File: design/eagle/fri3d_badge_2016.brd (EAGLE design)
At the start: 76.6 x 67.3 mm, 43 parts, among them Q1 MOSFET-NCHANNEL2N7002PW, U1 MCP73831

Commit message: added Fri3d Camp 2016 logo + silkscreen clean up
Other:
- board size 76.6 x 67.3 mm -> 76.5 x 67.4 mm
- board text removed: "Fri3d Camp 2016"

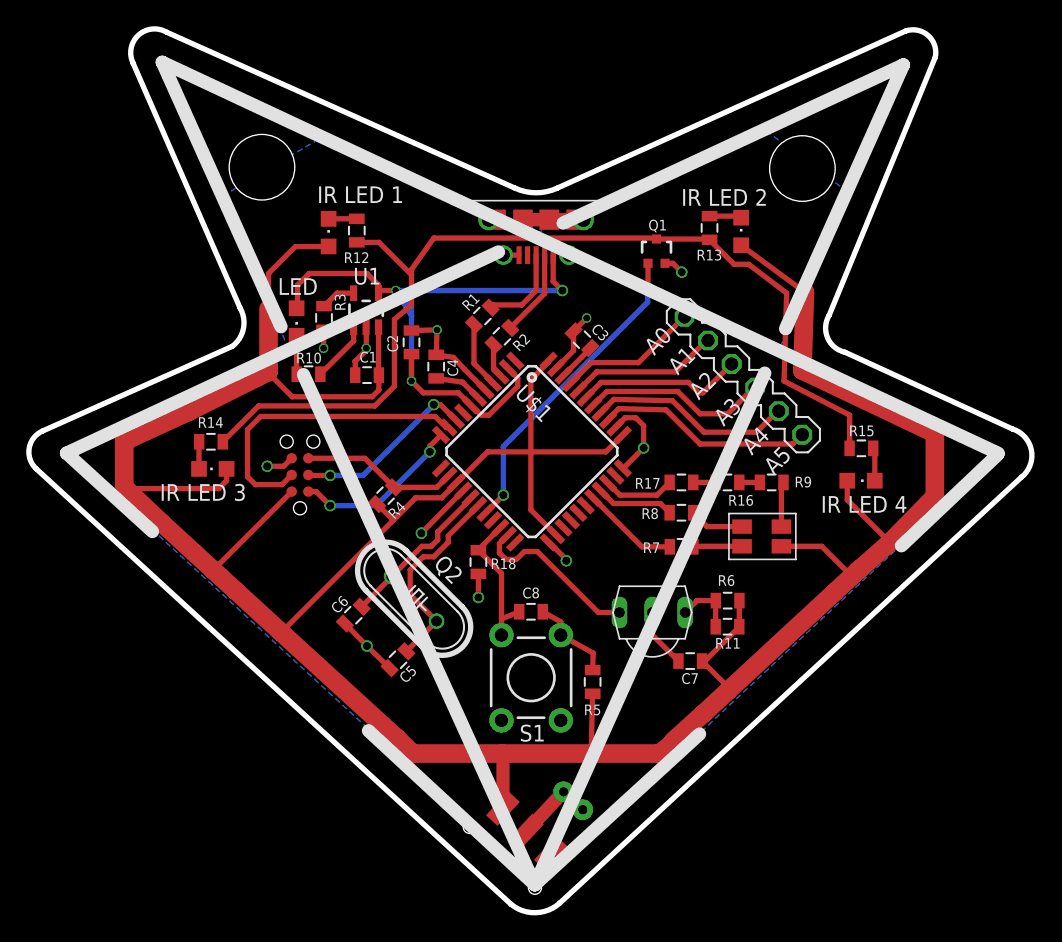
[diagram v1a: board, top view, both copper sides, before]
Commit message: IR powered by pin, added headers, cleaned up silk
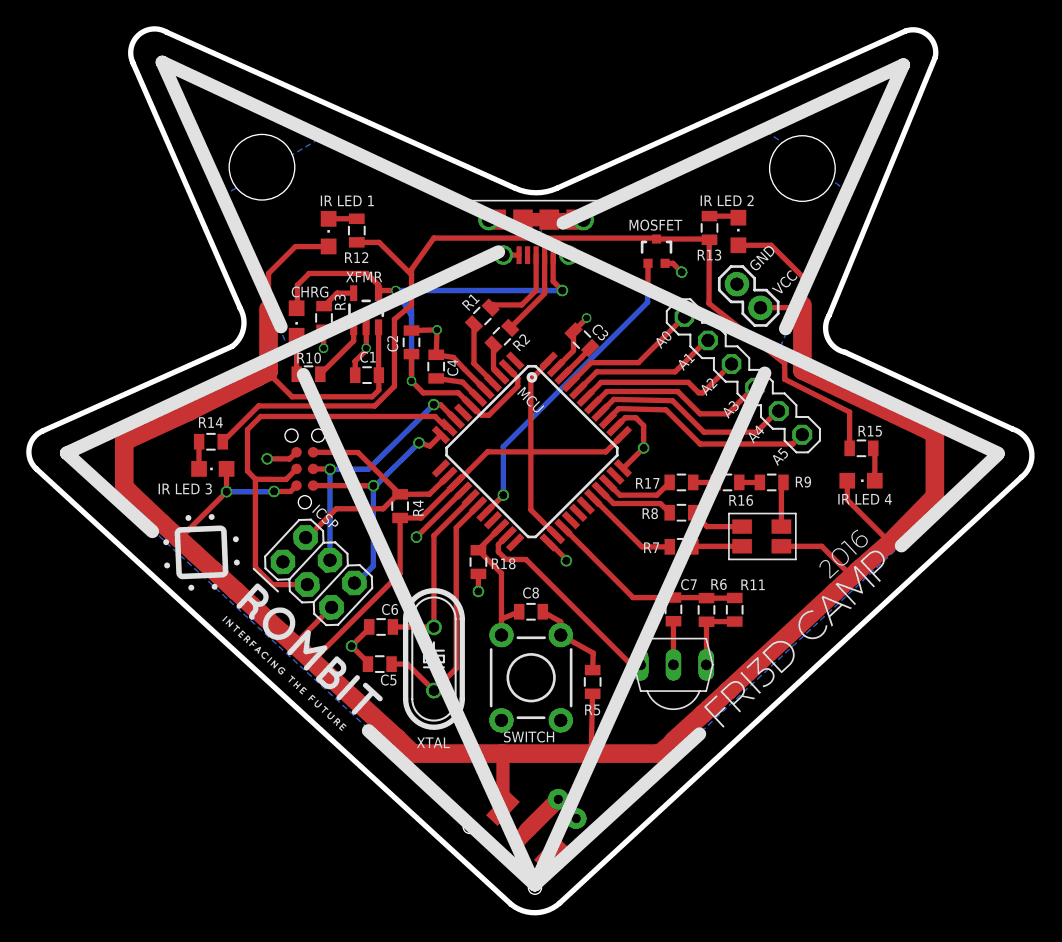
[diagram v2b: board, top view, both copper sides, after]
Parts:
- removed Q2: (no value), crystal:HC49/S
- added ICSP: (no value), SparkFun-Connectors:2X03
- added J2: (no value), SparkFun-Connectors:1X02
- added XTAL: (no value), crystal:HC49/S
- CHRGLED: value LED -> CHRG
- J3: device SparkFun-Connectors:JST-2-PTH-VERT -> SparkFun-Connectors:JST-2-PTH
- moved U$3 4.30 mm to (50.5, 19.4)
- moved C7 4.14 mm to (50.5, 23.6), turned to 270 degrees
- moved C6 2.30 mm to (28.2, 22.2), turned to 0 degrees
- moved R6 1.76 mm to (53.0, 23.6), turned to 90 degrees
- moved C5 1.43 mm to (28.1, 19.4), turned to 0 degrees
- moved R11 1.40 mm to (55.1, 23.6), turned to 90 degrees
- moved R4 1.37 mm to (29.6, 31.5), turned to 90 degrees
- moved J3 1.32 mm to (42.4, 8.38), turned to 47 degrees
- moved U$7 0.59 mm to (22.4, 31.8)
- moved LED2 0.21 mm to (55.4, 52.4)
- renumbered LED5 to CHRGLED, Q1 to MOSFET, S1 to SWITCH, U$1 to MCU, U1 to XFMR
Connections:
- new net IR_VCC: C7.1, MCU.25, R11.2, R6.2
- net GND: now also ICSP.1, J2.1
- net MISO: now also ICSP.6
- net MOSI: now also ICSP.3
- net N$8: now also XTAL.2; no longer Q2.2
- net N$9: now also XTAL.1; no longer Q2.1
- net RST: now also ICSP.2
- net SCK: now also ICSP.4
- net VCC: now also ICSP.5, J2.2; no longer C7.1, R11.2, R6.2
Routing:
- net IR_VCC: track 0.00 -> 15.3 mm
- net MOSI: track 23.6 -> 34.8 mm
- net RST: track 12.0 -> 20.8 mm
- net MISO: track 13.1 -> 19.6 mm
- net SCK: track 14.0 -> 20.5 mm
- net VCC: track 248.3 -> 242.2 mm, vias 0 -> 2
- net N$8: track 15.5 -> 19.6 mm
- net IR_RX: track 13.2 -> 16.0 mm
- net N$9: track 12.2 -> 14.2 mm
- net GND: track 53.3 -> 51.5 mm
- net N$10: track 4.71 -> 5.45 mm
- net N$17: track 4.09 -> 3.41 mm
- net N$24: track 75.8 -> 75.3 mm
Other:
- board text added: "GND"
- board text added: "VCC"
- board text added: "battery"

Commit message: attached IR/MOSFET to correct pin for IRremote
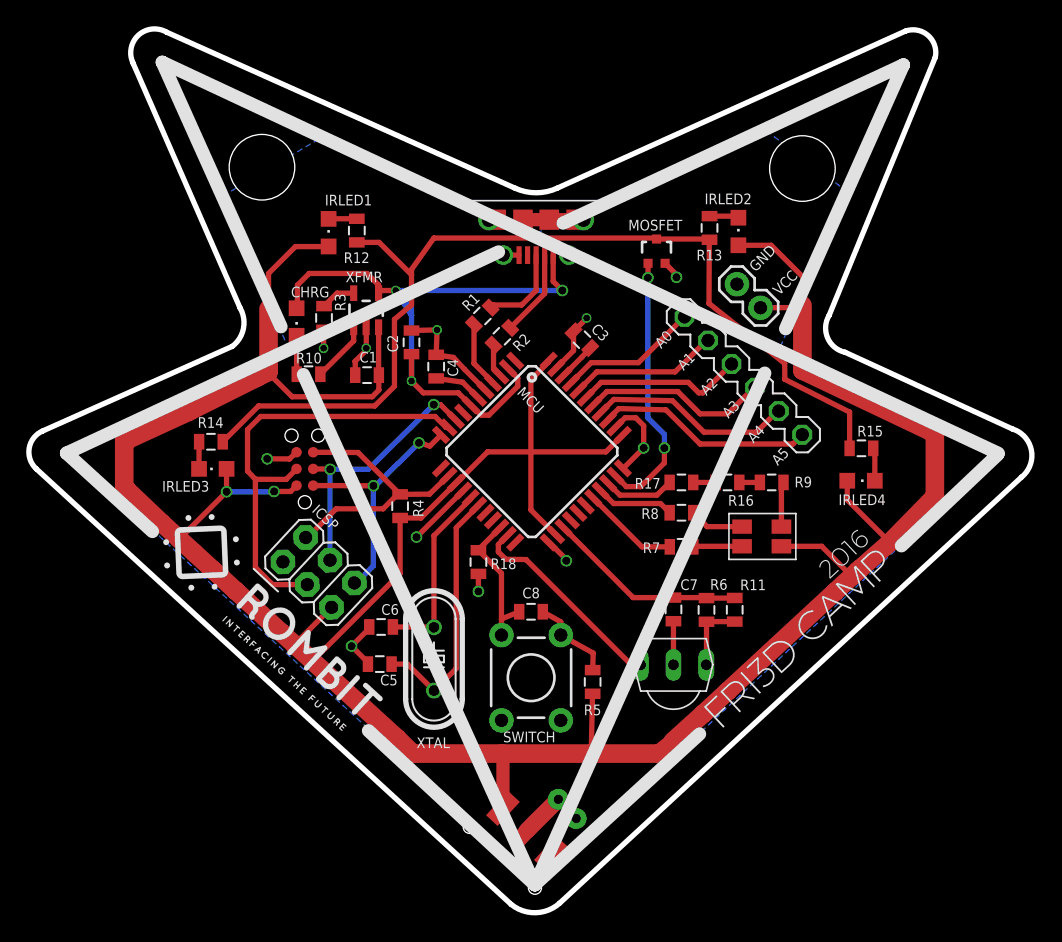
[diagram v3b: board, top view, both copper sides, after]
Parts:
- IRLED1: value IR LED 1 -> (none)
- IRLED2: value IR LED 2 -> (none)
- IRLED3: value IR LED 3 -> (none)
- IRLED4: value IR LED 4 -> (none)
- renumbered LED1 to IRLED1, LED2 to IRLED2, LED3 to IRLED3, LED4 to IRLED4
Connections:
- net IR_TX: now also MCU.32; no longer MCU.18
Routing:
- net IR_TX: track 24.2 -> 20.6 mm
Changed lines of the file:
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@@
 <attribute name="NAME" x="38.948" y="24.4355" size="0.8128" layer="25"/>
 </element>
-<element name="LED1" library="led" package="CHIPLED_0805" value="IR LED 1" x="24.18" y="52.31" smashed="yes">
-<attribute name="VALUE" x="27.72" y="55.14" size="0.8128" layer="25" rot="R180"/>
-</element>
-<element name="LED2" library="led" package="CHIPLED_0805" value="IR LED 2" x="55.42" y="52.4" smashed="yes">
-<attribute name="VALUE" x="56.68" y="55.15" size="0.8128" layer="25" rot="R180"/>
-</element>
-<element name="LED3" library="led" package="CHIPLED_0805" value="IR LED 3" x="15.35" y="34.3" smashed="yes" rot="R90">
-<attribute name="VALUE" x="15.36" y="33.18" size="0.8128" layer="25" rot="R180"/>
-</element>
-<element name="LED4" library="led" package="CHIPLED_0805" value="IR LED 4" x="64.77" y="33.4" smashed="yes" rot="R270">
-<attribute name="VALUE" x="62.94" y="31.58" size="0.8128" layer="25"/>
+<element name="IRLED1" library="led" package="CHIPLED_0805" value="" x="24.18" y="52.31" smashed="yes">
+<attribute name="NAME" x="27.49" y="55.2" size="0.8128" layer="25" rot="R180"/>
+<attribute name="VALUE" x="26.72" y="51.04" size="1.27" layer="27" rot="R90"/>
+</element>
+<element name="IRLED2" library="led" package="CHIPLED_0805" value="" x="55.42" y="52.4" smashed="yes">
+<attribute name="NAME" x="56.44" y="55.29" size="0.8128" layer="25" rot="R180"/>
+<attribute name="VALUE" x="57.96" y="51.13" size="1.27" layer="27" rot="R90"/>
+</element>
+<element name="IRLED3" library="led" package="CHIPLED_0805" value="" x="15.35" y="34.3" smashed="yes" rot="R90">
+<attribute name="NAME" x="15.08" y="33.38" size="0.8128" layer="25" rot="R180"/>
+</element>
+<element name="IRLED4" library="led" package="CHIPLED_0805" value="" x="64.77" y="33.4" smashed="yes" rot="R270">
+<attribute name="NAME" x="63.05" y="31.54" size="0.8128" layer="25"/>
+<attribute name="VALUE" x="63.5" y="30.86" size="1.27" layer="27"/>
 </element>
 <element name="CHRGLED" library="adafruit" package="CHIPLED_0805" value="CHRG" x="21.74" y="45.5" smashed="yes" rot="R180">
@@
 </polygon>
 <wire x1="41.009646875" y1="28.690353125" x2="40.952790625" y2="28.690353125" width="0.4064" layer="1"/>
-<via x="51.1" y="49.3" extent="1-16" drill="0.6"/>
 <wire x1="34.447409375" y1="32.65015" x2="30.88" y2="29.1" width="0.4064" layer="1"/>
 <via x="30.88" y="29.1" extent="1-16" drill="0.6"/>
@@
 <wire x1="26.2" y1="42.5" x2="26.21" y2="42.5" width="0.4064" layer="1"/>
 <wire x1="26.21" y1="42.5" x2="26.21" y2="41.45" width="0.4064" layer="1"/>
-<wire x1="49.83" y1="49.975" x2="50.425" y2="49.975" width="0.4064" layer="1"/>
-<wire x1="50.425" y1="49.975" x2="51.1" y2="49.3" width="0.4064" layer="1"/>
 <contactref element="U$7" pad="P$4"/>
 <wire x1="21.735" y1="35.57" x2="21.195" y2="35.06" width="0.4064" layer="1"/>
@@
 <wire x1="27.18" y1="19.42" x2="27.18" y2="19.54" width="0.4064" layer="1"/>
 <wire x1="27.18" y1="19.54" x2="25.93" y2="20.79" width="0.4064" layer="1"/>
+<wire x1="49.83" y1="49.975" x2="50.7" y2="49.105" width="0.4064" layer="1"/>
+<wire x1="50.7" y1="49.105" x2="50.7" y2="48.91" width="0.4064" layer="1"/>
+<via x="50.7" y="48.91" extent="1-16" drill="0.6"/>
 </signal>
 <signal name="D+">
@@
 <wire x1="52.740425" y1="15.632146875" x2="50.43818125" y2="13.550684375" width="1.4224" layer="1"/>
 <wire x1="70.4" y1="32.2" x2="66.97093125" y2="28.692396875" width="1.4224" layer="1"/>
-<contactref element="LED4" pad="A"/>
-<contactref element="LED3" pad="A"/>
-<contactref element="LED2" pad="A"/>
-<contactref element="LED1" pad="A"/>
+<contactref element="IRLED4" pad="A"/>
+<contactref element="IRLED3" pad="A"/>
+<contactref element="IRLED2" pad="A"/>
+<contactref element="IRLED1" pad="A"/>
 <wire x1="66.97093125" y1="28.692396875" x2="64.525525" y2="26.538534375" width="1.4224" layer="1"/>
 <wire x1="19.6" y1="46.5" x2="19.6" y2="49.2" width="0.4064" layer="1"/>
@@
 <signal name="IR_TX">
 <contactref element="MOSFET" pad="1"/>
-<contactref element="MCU" pad="18"/>
-<wire x1="48.5" y1="47" x2="48.5" y2="48.1" width="0.4064" layer="16"/>
-<via x="48.5" y="48.1" extent="1-16" drill="0.6"/>
-<wire x1="36.144465625" y1="30.95309375" x2="36.15309375" y2="30.95309375" width="0.4064" layer="1"/>
-<wire x1="36.15309375" y1="30.95309375" x2="37.5" y2="32.3" width="0.4064" layer="1"/>
-<via x="37.5" y="32.3" extent="1-16" drill="0.6"/>
-<wire x1="37.5" y1="32.3" x2="37.5" y2="36" width="0.4064" layer="16"/>
-<wire x1="37.5" y1="36" x2="48.5" y2="47" width="0.4064" layer="16"/>
-<wire x1="48.53" y1="49.975" x2="48.53" y2="48.13" width="0.4064" layer="1"/>
-<wire x1="48.53" y1="48.13" x2="48.5" y2="48.1" width="0.4064" layer="1"/>
+<contactref element="MCU" pad="32"/>
+<wire x1="46.043959375" y1="33.781521875" x2="46.87548125" y2="32.95" width="0.4064" layer="1"/>
+<wire x1="46.87548125" y1="32.95" x2="47.97" y2="32.95" width="0.4064" layer="1"/>
+<wire x1="47.97" y1="32.95" x2="49.78" y2="34.76" width="0.4064" layer="1"/>
+<via x="49.78" y="35.89" extent="1-16" drill="0.6"/>
+<wire x1="49.78" y1="36.93" x2="48.52" y2="38.19" width="0.4064" layer="16"/>
+<wire x1="48.52" y1="38.19" x2="48.52" y2="48.87" width="0.4064" layer="16"/>
+<via x="48.52" y="48.87" extent="1-16" drill="0.6"/>
+<wire x1="48.52" y1="48.87" x2="48.53" y2="48.88" width="0.4064" layer="1"/>
+<wire x1="48.53" y1="48.88" x2="48.53" y2="49.975" width="0.4064" layer="1"/>
+<wire x1="49.78" y1="36.93" x2="49.78" y2="35.89" width="0.4064" layer="16"/>
+<wire x1="49.78" y1="34.76" x2="49.78" y2="35.89" width="0.4064" layer="1"/>
 </signal>
 <signal name="BUTTON">
@@
 <signal name="N$13">
 <contactref element="R12" pad="2"/>
-<contactref element="LED1" pad="C"/>
+<contactref element="IRLED1" pad="C"/>
 <wire x1="24.18" y1="53.36" x2="24.39" y2="53.37" width="0.4064" layer="1"/>
 <wire x1="24.39" y1="53.37" x2="26.33" y2="53.37" width="0.4064" layer="1"/>
@@
 <signal name="N$14">
 <contactref element="R13" pad="2"/>
-<contactref element="LED2" pad="C"/>
+<contactref element="IRLED2" pad="C"/>
 <wire x1="53.22" y1="53.57" x2="55.63" y2="53.57" width="0.4064" layer="1"/>
 <wire x1="55.63" y1="53.57" x2="55.42" y2="53.45" width="0.4064" layer="1"/>
@@
 <signal name="N$15">
 <contactref element="R14" pad="2"/>
-<contactref element="LED3" pad="C"/>
+<contactref element="IRLED3" pad="C"/>
 <wire x1="14.31" y1="36.37" x2="14.3" y2="36.36" width="0.4064" layer="1"/>
 <wire x1="14.3" y1="36.36" x2="14.3" y2="34.3" width="0.4064" layer="1"/>
@@
 <signal name="N$16">
 <contactref element="R15" pad="2"/>
-<contactref element="LED4" pad="C"/>
+<contactref element="IRLED4" pad="C"/>
 <wire x1="65.82" y1="33.4" x2="65.82" y2="35.75" width="0.4064" layer="1"/>
 <wire x1="65.82" y1="35.75" x2="65.7" y2="35.87" width="0.4064" layer="1"/>
